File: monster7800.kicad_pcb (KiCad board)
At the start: 2 copper layers, 33 x 57 mm, 5 parts, among them J1 Conn_01x09, J2 DB9_Female_MountingHoles

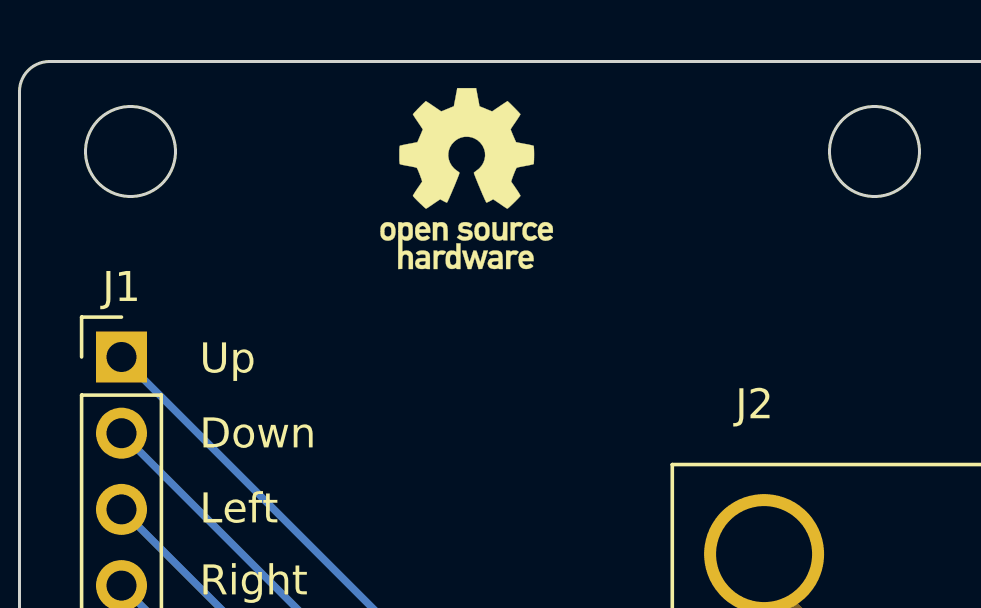
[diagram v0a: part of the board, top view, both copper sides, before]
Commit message: add reference to github page on PCB
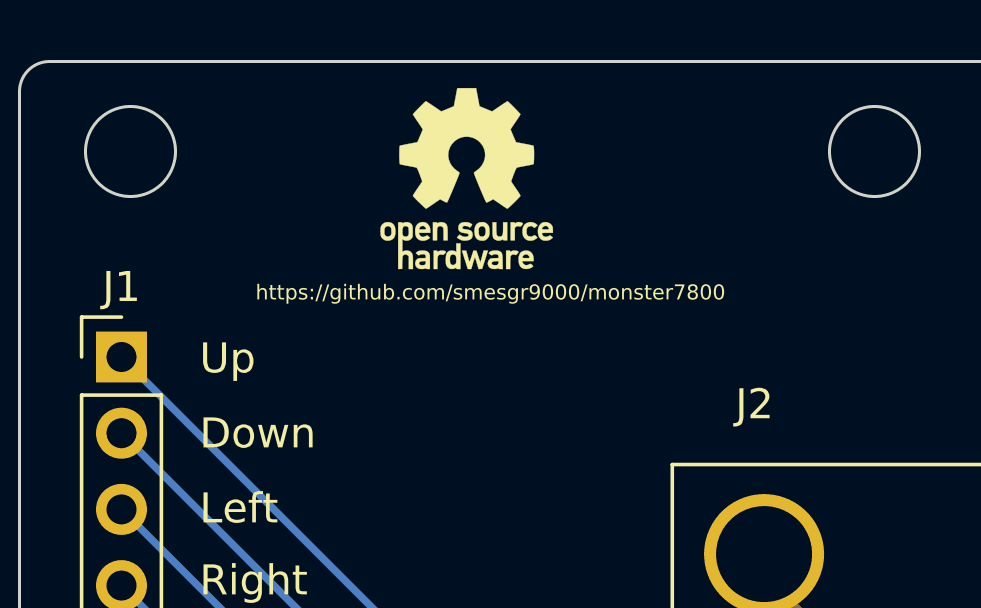
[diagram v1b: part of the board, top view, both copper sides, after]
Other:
- board text added: "https://github.com/smesgr9000/monster7800"
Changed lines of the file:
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@@
     (effects (font (size 1 1) (thickness 0.15)) (justify left))
+  )
+  (gr_text "https://github.com/smesgr9000/monster7800" (at 235.7 63.7) (layer "F.SilkS")
+    (effects (font (size 0.5 0.5) (thickness 0.1)))
   )
   (gr_text "GND" (at 226 76) (layer "F.SilkS")
